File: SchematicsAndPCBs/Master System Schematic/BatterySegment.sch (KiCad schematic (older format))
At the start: 148 parts

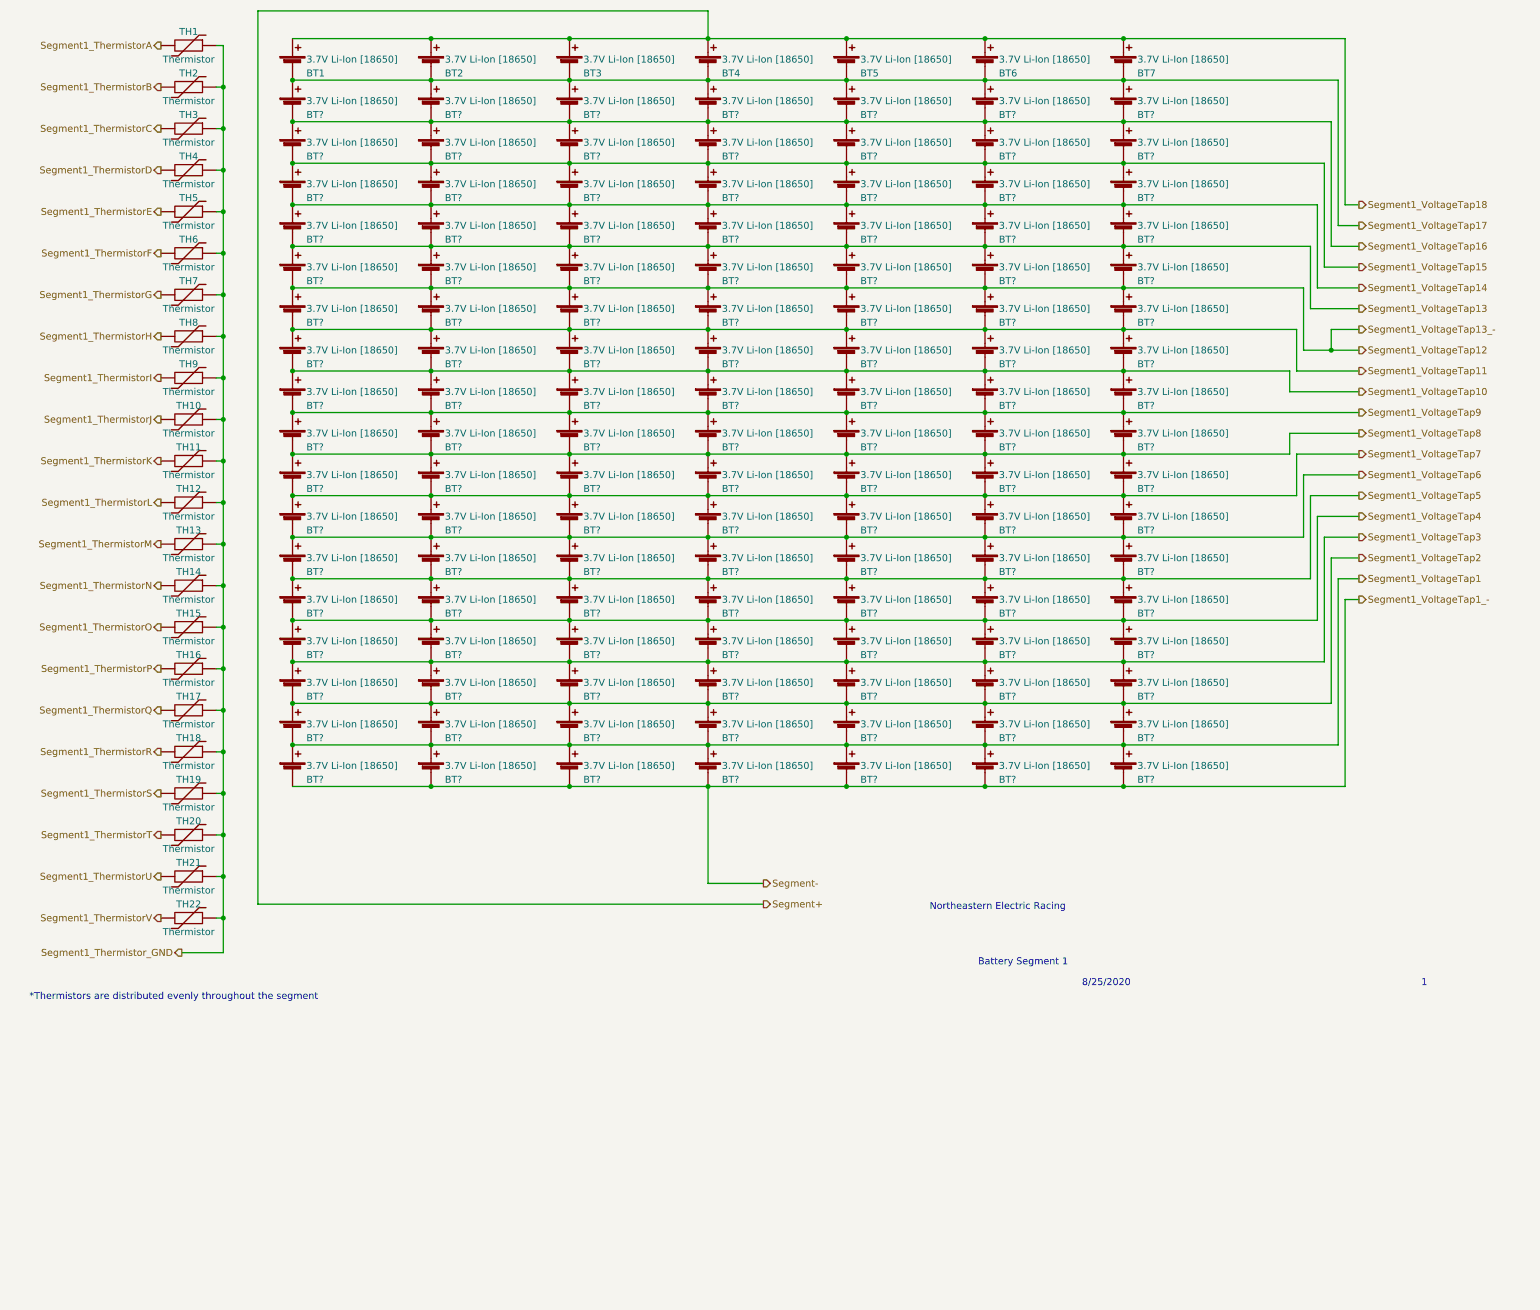
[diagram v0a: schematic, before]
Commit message: Paper Size and Title Blocks
-Switched all paper sizes over to America units  (letter size A and tabloid size B) (so we can actually be cool and print them an stuff)
-Fixed title blocks to use sheet properties
-Started some changes to the accumulator segment schematic
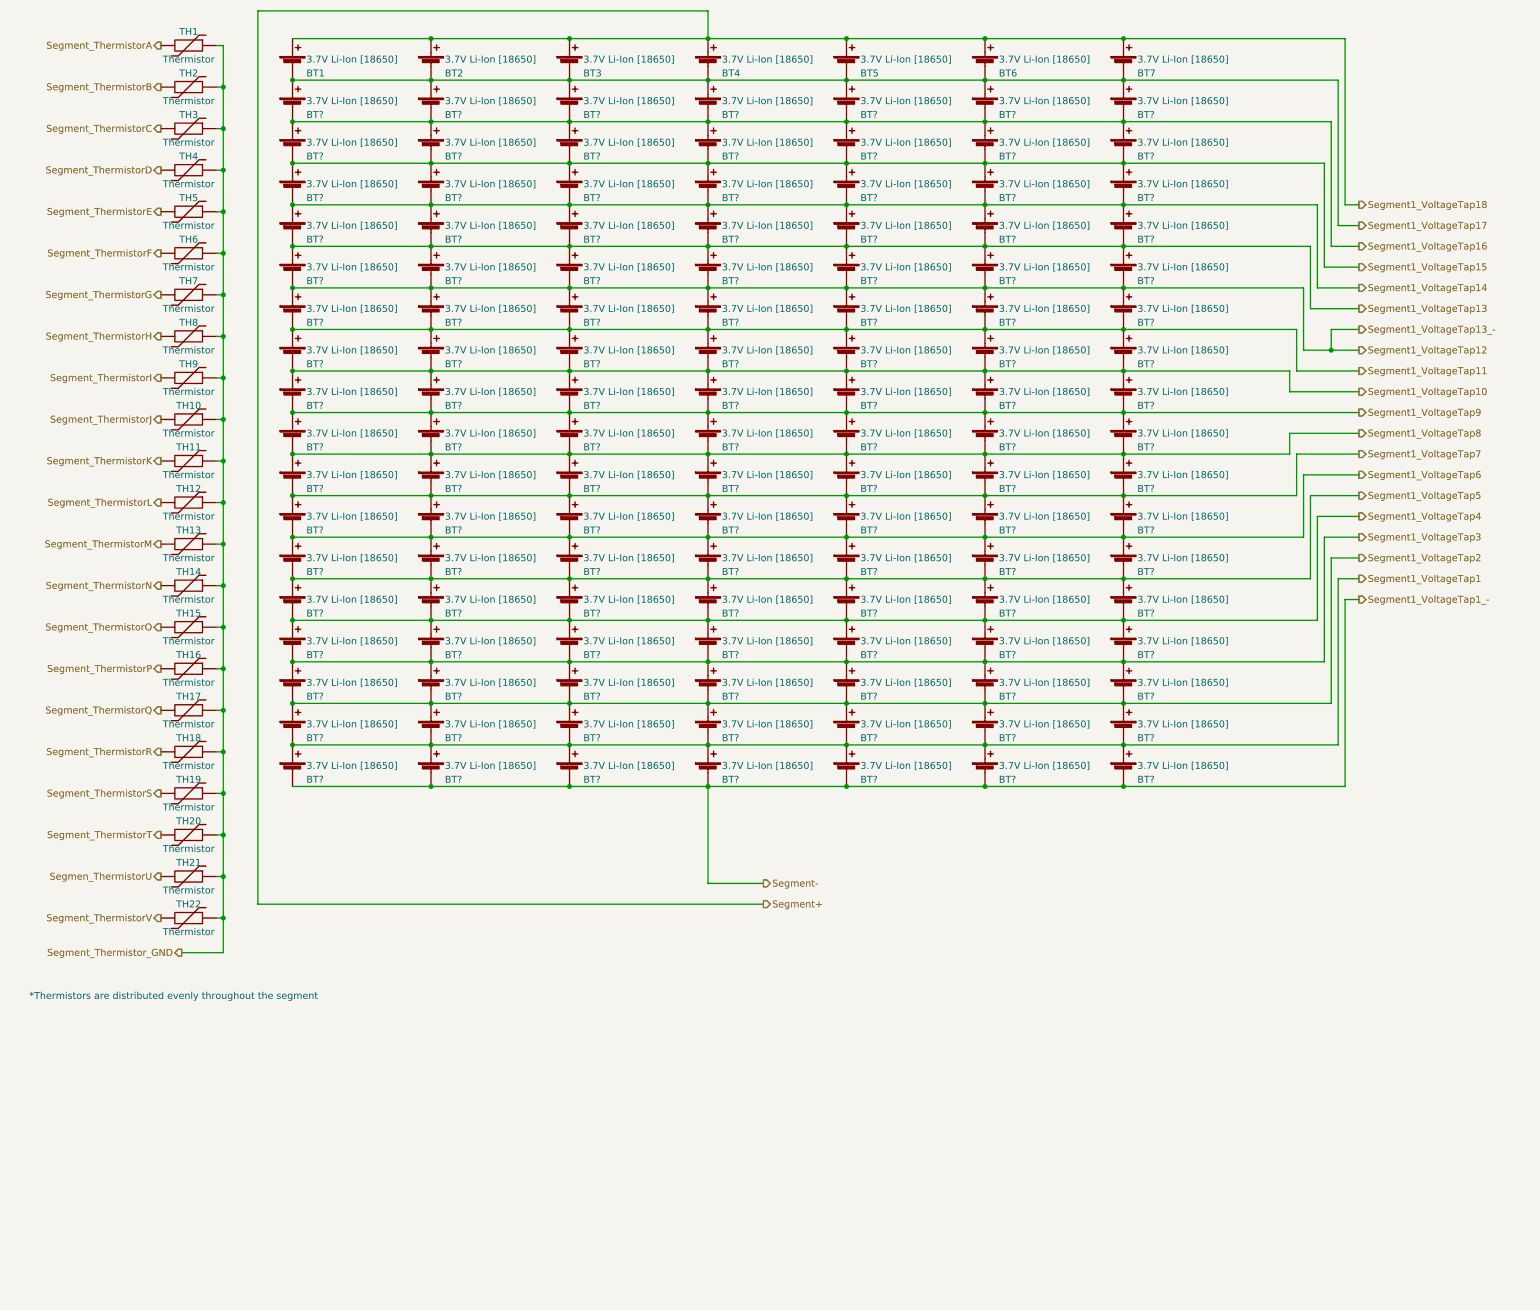
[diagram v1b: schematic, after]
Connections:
- net Segment1_ThermistorA renamed Segment_ThermistorA
- net Segment1_ThermistorB renamed Segment_ThermistorB
- net Segment1_ThermistorC renamed Segment_ThermistorC
- net Segment1_ThermistorD renamed Segment_ThermistorD
- net Segment1_ThermistorE renamed Segment_ThermistorE
- net Segment1_ThermistorF renamed Segment_ThermistorF
- net Segment1_ThermistorG renamed Segment_ThermistorG
- net Segment1_ThermistorH renamed Segment_ThermistorH
- net Segment1_ThermistorI renamed Segment_ThermistorI
- net Segment1_ThermistorJ renamed Segment_ThermistorJ
- net Segment1_ThermistorK renamed Segment_ThermistorK
- net Segment1_ThermistorL renamed Segment_ThermistorL
- net Segment1_ThermistorM renamed Segment_ThermistorM
- net Segment1_ThermistorN renamed Segment_ThermistorN
- net Segment1_ThermistorO renamed Segment_ThermistorO
- net Segment1_ThermistorP renamed Segment_ThermistorP
- net Segment1_ThermistorQ renamed Segment_ThermistorQ
- net Segment1_ThermistorR renamed Segment_ThermistorR
- net Segment1_ThermistorS renamed Segment_ThermistorS
- net Segment1_ThermistorT renamed Segment_ThermistorT
- net Segment1_ThermistorU renamed Segmen_ThermistorU
- net Segment1_ThermistorV renamed Segment_ThermistorV
- net Segment1_Thermistor_GND renamed Segment_Thermistor_GND
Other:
- note removed: "1"
- note removed: "8/25/2020"
- note removed: "Battery Segment 1"
- note removed: "Northeastern Electric Racing"
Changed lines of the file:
@@
 EELAYER 30 0
 EELAYER END
-$Descr A4 11693 8268
+$Descr B 17000 11000
 encoding utf-8
 Sheet 8 8
-Title ""
-Date ""
-Rev ""
-Comp ""
+Title "Accumulator Segment"
+Date "2020-09-17"
+Rev "2"
+Comp "Northeastern Electric Racing"
 Comment1 ""
 Comment2 ""
@@
 Segment-
 Text HLabel 1450 850  0    50   Output ~ 0
-Segment1_ThermistorA
+Segment_ThermistorA
 Text HLabel 1450 1150 0    50   Output ~ 0
-Segment1_ThermistorB
+Segment_ThermistorB
 Text HLabel 1450 1450 0    50   Output ~ 0
-Segment1_ThermistorC
+Segment_ThermistorC
 Text HLabel 1450 1750 0    50   Output ~ 0
-Segment1_ThermistorD
+Segment_ThermistorD
 Text HLabel 10100 4850 2    50   Output ~ 0
 Segment1_VoltageTap1_-
@@
 $EndComp
 Text HLabel 1450 2050 0    50   Output ~ 0
-Segment1_ThermistorE
+Segment_ThermistorE
 Text HLabel 1450 2350 0    50   Output ~ 0
-Segment1_ThermistorF
+Segment_ThermistorF
 Text HLabel 1450 2650 0    50   Output ~ 0
-Segment1_ThermistorG
+Segment_ThermistorG
 Text HLabel 1450 2950 0    50   Output ~ 0
-Segment1_ThermistorH
+Segment_ThermistorH
 $Comp
 L Device:Thermistor TH5
@@
 $EndComp
 Text HLabel 1450 3250 0    50   Output ~ 0
-Segment1_ThermistorI
+Segment_ThermistorI
 Text HLabel 1450 3550 0    50   Output ~ 0
-Segment1_ThermistorJ
+Segment_ThermistorJ
 Text HLabel 1450 3850 0    50   Output ~ 0
-Segment1_ThermistorK
+Segment_ThermistorK
 Text HLabel 1450 4150 0    50   Output ~ 0
-Segment1_ThermistorL
+Segment_ThermistorL
 $Comp
 L Device:Thermistor TH9
@@
 $EndComp
 Text HLabel 1450 4450 0    50   Output ~ 0
-Segment1_ThermistorM
+Segment_ThermistorM
 Text HLabel 1450 4750 0    50   Output ~ 0
-Segment1_ThermistorN
+Segment_ThermistorN
 Text HLabel 1450 5050 0    50   Output ~ 0
-Segment1_ThermistorO
+Segment_ThermistorO
 Text HLabel 1450 5350 0    50   Output ~ 0
-Segment1_ThermistorP
+Segment_ThermistorP
 $Comp
 L Device:Thermistor TH13
@@
 $EndComp
 Text HLabel 1450 5650 0    50   Output ~ 0
-Segment1_ThermistorQ
+Segment_ThermistorQ
 Text HLabel 1450 5950 0    50   Output ~ 0
-Segment1_ThermistorR
+Segment_ThermistorR
 $Comp
 L Device:Thermistor TH17
@@
 $EndComp
 Text HLabel 1450 6250 0    50   Output ~ 0
-Segment1_ThermistorS
+Segment_ThermistorS
 Text HLabel 1450 6850 0    50   Output ~ 0
-Segment1_ThermistorU
+Segmen_ThermistorU
 Text HLabel 1450 7150 0    50   Output ~ 0
-Segment1_ThermistorV
+Segment_ThermistorV
 $Comp
 L Device:Thermistor TH20
@@
 $EndComp
 Text HLabel 1600 7400 0    50   Output ~ 0
-Segment1_Thermistor_GND
+Segment_Thermistor_GND
 Text HLabel 1450 6550 0    50   Output ~ 0
-Segment1_ThermistorT
+Segment_ThermistorT
 Wire Wire Line
 	1850 850  1900 850
@@
 Wire Wire Line
 	2150 600  2150 7050
-Text Notes 7350 7500 0    50   ~ 0
-Battery Segment 1
-Text Notes 8100 7650 0    50   ~ 0
-8/25/2020
-Text Notes 10550 7650 0    50   ~ 0
-1
-Text Notes 7000 7100 0    50   ~ 0
-Northeastern Electric Racing
 Text Notes 500  7750 0    50   ~ 0
 *Thermistors are distributed evenly throughout the segment

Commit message: Therms and Volt Taps
Mostly fixed all thermistor and volt taps
Also created new sheet for BMS container and updated library part for OrionThermExpansionModule
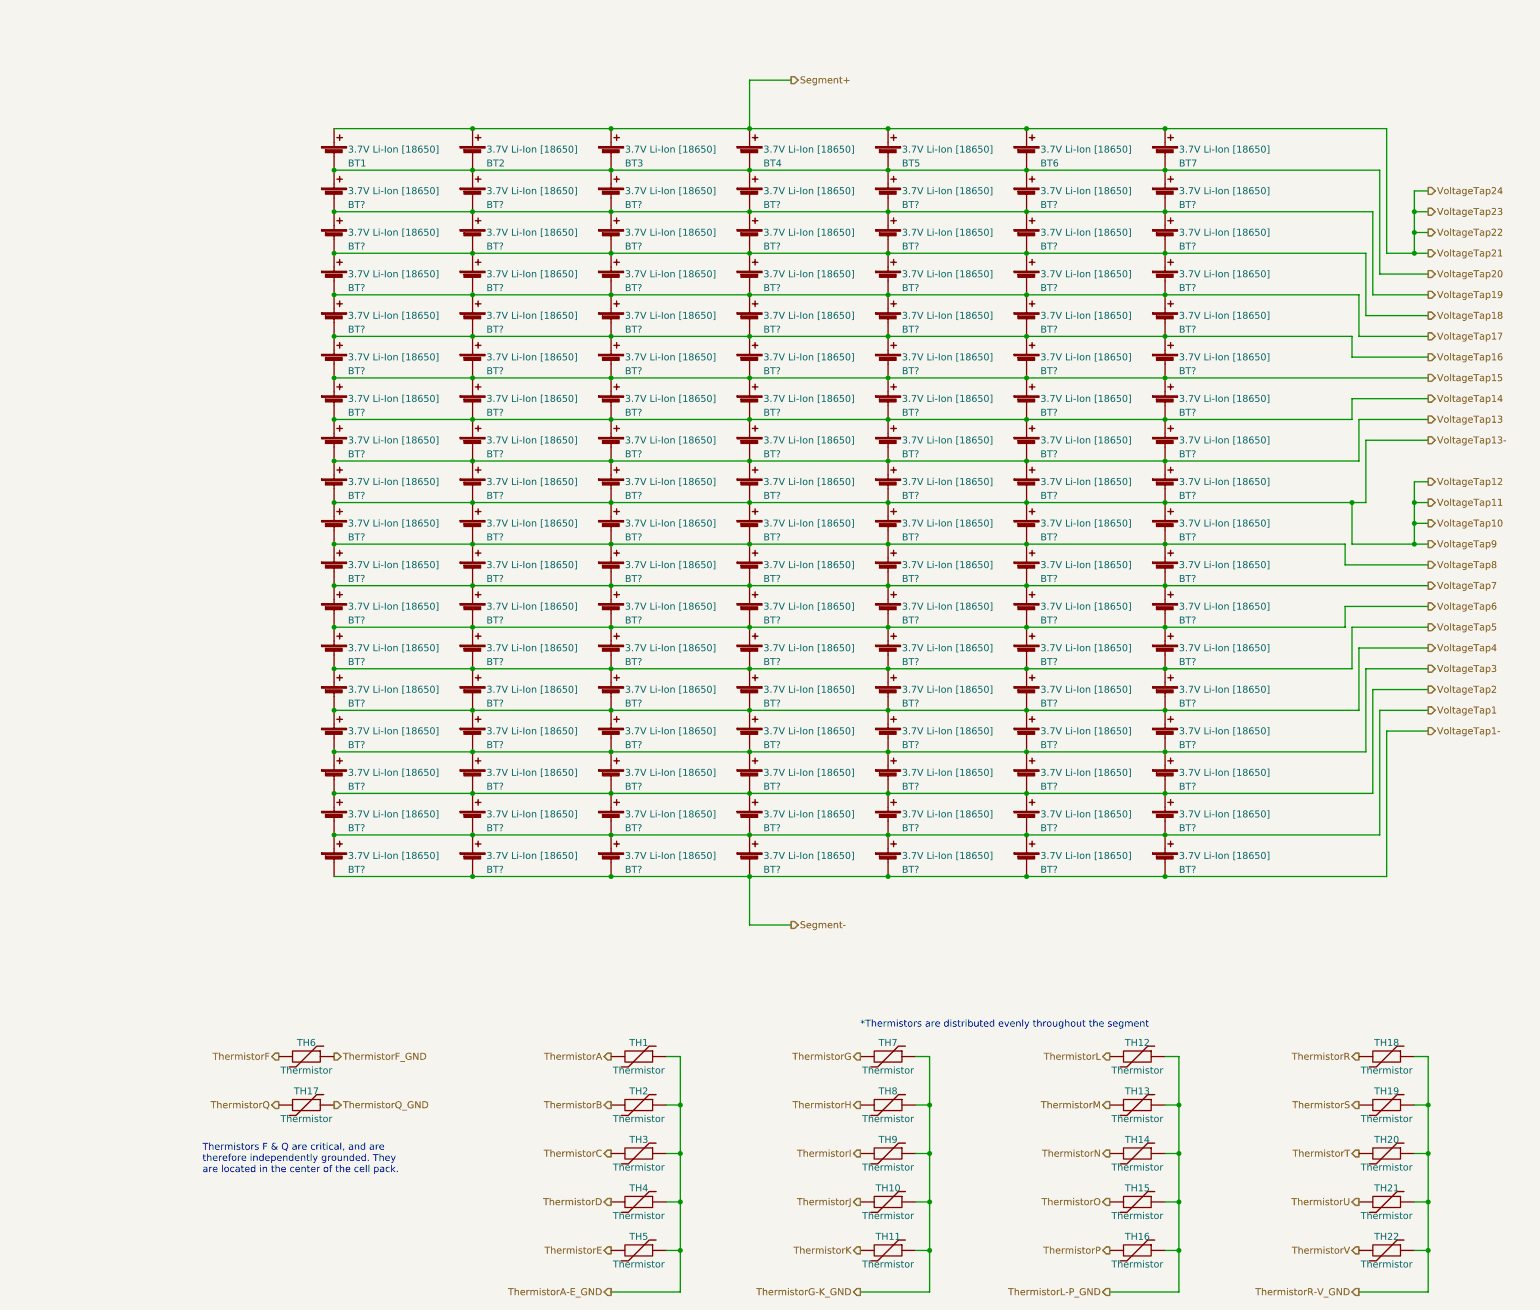
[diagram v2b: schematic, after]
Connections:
- net Segmen_ThermistorU renamed ThermistorU
- net Segment1_VoltageTap1 renamed VoltageTap1
- net Segment1_VoltageTap10 renamed VoltageTap13
- net Segment1_VoltageTap11 renamed VoltageTap14
- net Segment1_VoltageTap12 renamed VoltageTap15
- net Segment1_VoltageTap13 renamed VoltageTap16
- net Segment1_VoltageTap14 renamed VoltageTap17
- net Segment1_VoltageTap15 renamed VoltageTap18
- net Segment1_VoltageTap16 renamed VoltageTap19
- net Segment1_VoltageTap17 renamed VoltageTap20
- net Segment1_VoltageTap2 renamed VoltageTap2
- net Segment1_VoltageTap3 renamed VoltageTap3
- net Segment1_VoltageTap4 renamed VoltageTap4
- net Segment1_VoltageTap5 renamed VoltageTap5
- net Segment1_VoltageTap6 renamed VoltageTap6
- net Segment1_VoltageTap7 renamed VoltageTap7
- net Segment1_VoltageTap8 renamed VoltageTap8
- net Segment1_VoltageTap9 renamed VoltageTap10
- net Segment_ThermistorA renamed ThermistorA
- net Segment_ThermistorB renamed ThermistorB
- net Segment_ThermistorC renamed ThermistorC
- net Segment_ThermistorD renamed ThermistorD
- net Segment_ThermistorE renamed ThermistorE
- net Segment_ThermistorF renamed ThermistorF
- net Segment_ThermistorG renamed ThermistorG
- net Segment_ThermistorH renamed ThermistorH
- net Segment_ThermistorI renamed ThermistorI
- net Segment_ThermistorJ renamed ThermistorJ
- net Segment_ThermistorK renamed ThermistorK
- net Segment_ThermistorL renamed ThermistorL
- net Segment_ThermistorM renamed ThermistorM
- net Segment_ThermistorN renamed ThermistorN
- net Segment_ThermistorO renamed ThermistorO
- net Segment_ThermistorP renamed ThermistorP
- net Segment_ThermistorQ renamed ThermistorQ
- net Segment_ThermistorR renamed ThermistorR
- net Segment_ThermistorS renamed ThermistorS
- net Segment_ThermistorT renamed ThermistorT
- net Segment_ThermistorV renamed ThermistorV
- removed net Segment_Thermistor_GND: TH1.1, TH10.1, TH11.1, TH12.1, TH13.1, TH14.1, TH15.1, TH16.1, TH17.1, TH18.1, TH19.1, TH2.1, TH20.1, TH21.1, TH22.1, TH3.1, TH4.1, TH5.1, TH6.1, TH7.1, TH8.1, TH9.1
- new net ThermistorA-E_GND: TH1.1, TH2.1, TH3.1, TH4.1, TH5.1
- new net ThermistorF_GND: TH6.1
- new net ThermistorG-K_GND: TH10.1, TH11.1, TH7.1, TH8.1, TH9.1
- new net ThermistorL-P_GND: TH12.1, TH13.1, TH14.1, TH15.1, TH16.1
- new net ThermistorQ_GND: TH17.1
- new net ThermistorR-V_GND: TH18.1, TH19.1, TH20.1, TH21.1, TH22.1
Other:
- note added: "Thermistors F & Q are critical, and are\ntherefore independently grounded. They\nare located in the center of the cell pack."
- moved on the sheet: BT1, BT2, BT3, BT4, BT5, BT6, BT7, BT?, TH1, TH10, TH11, TH12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
